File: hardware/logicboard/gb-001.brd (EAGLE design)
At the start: 100 x 76 mm, 4 parts

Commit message: Good one.
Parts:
- removed SV2: (no value), con-ml:ML20L
- moved U$1 41.7 mm to (50.0, 38.0)
- moved SV3 26.0 mm to (50.0, 65.0)
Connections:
- new net GND: SV0.10, SV0.12, SV0.14, SV0.16, SV0.18, SV0.2, SV0.20, SV0.22, SV0.24, SV0.26, SV0.28, SV0.30, SV0.32, SV0.34, SV0.4, SV0.6, SV0.8, SV3.5
- new net NC: SV0.17
- new net T00: SV0.1, SV3.1
- new net T01: SV0.3, SV3.3
- new net T02: SV0.5, SV3.7
- new net T03: SV0.7, SV3.9
- new net T04: SV0.9, SV3.11
- new net T05: SV0.11, SV3.2
- new net T06: SV0.13, SV3.4
- new net T07: SV0.15, SV3.6
- new net T08: SV0.19, SV3.8
- new net T09: SV0.21, SV3.10
- new net T10: SV0.23, SV3.12
- new net T11: SV0.25, SV3.14
- new net T12: SV0.27
- new net T13: SV0.29
- new net T14: SV0.31
- new net T15: SV0.33
- new net VT: SV3.13
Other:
- board text added: "GeekBox 0.0.1-A"
- board text removed: "Pineapple IId 0.0.2-B"

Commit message: Routed.
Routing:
- net GND: track 0.00 -> 96.3 mm
- net T00: track 0.00 -> 74.2 mm
- net T10: track 0.00 -> 70.1 mm
- net T11: track 0.00 -> 69.3 mm
- net T07: track 0.00 -> 65.9 mm
- net T01: track 0.00 -> 65.5 mm
- net T05: track 0.00 -> 63.5 mm
- net T02: track 0.00 -> 60.9 mm
- net T09: track 0.00 -> 60.4 mm
- net T06: track 0.00 -> 59.1 mm
- net T03: track 0.00 -> 55.7 mm
- net T08: track 0.00 -> 55.1 mm
- net T04: track 0.00 -> 53.6 mm

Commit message: Added extra pins.
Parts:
- added JP1: (no value), pinhead:2X04
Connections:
- net GND: now also JP1.2, JP1.4, JP1.6, JP1.8
- net T12: now also JP1.1
- net T13: now also JP1.3
- net T14: now also JP1.5
- net T15: now also JP1.7
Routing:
- net T14: track 0.00 -> 62.4 mm
- net T13: track 0.00 -> 57.5 mm
- net T15: track 0.00 -> 53.4 mm, vias 0 -> 1
- net T12: track 0.00 -> 47.1 mm
- net GND: track 96.3 -> 120.5 mm
- net T07: track 65.9 -> 56.1 mm
- net T11: track 69.3 -> 77.2 mm
- net T01: track 65.5 -> 72.6 mm
- net T10: track 70.1 -> 63.8 mm
- net T06: track 59.1 -> 64.7 mm, vias 0 -> 1
- net T03: track 55.7 -> 58.8 mm
- net T00: track 74.2 -> 76.2 mm
- net T05: track 63.5 -> 65.2 mm
- net T02: track 60.9 -> 62.4 mm

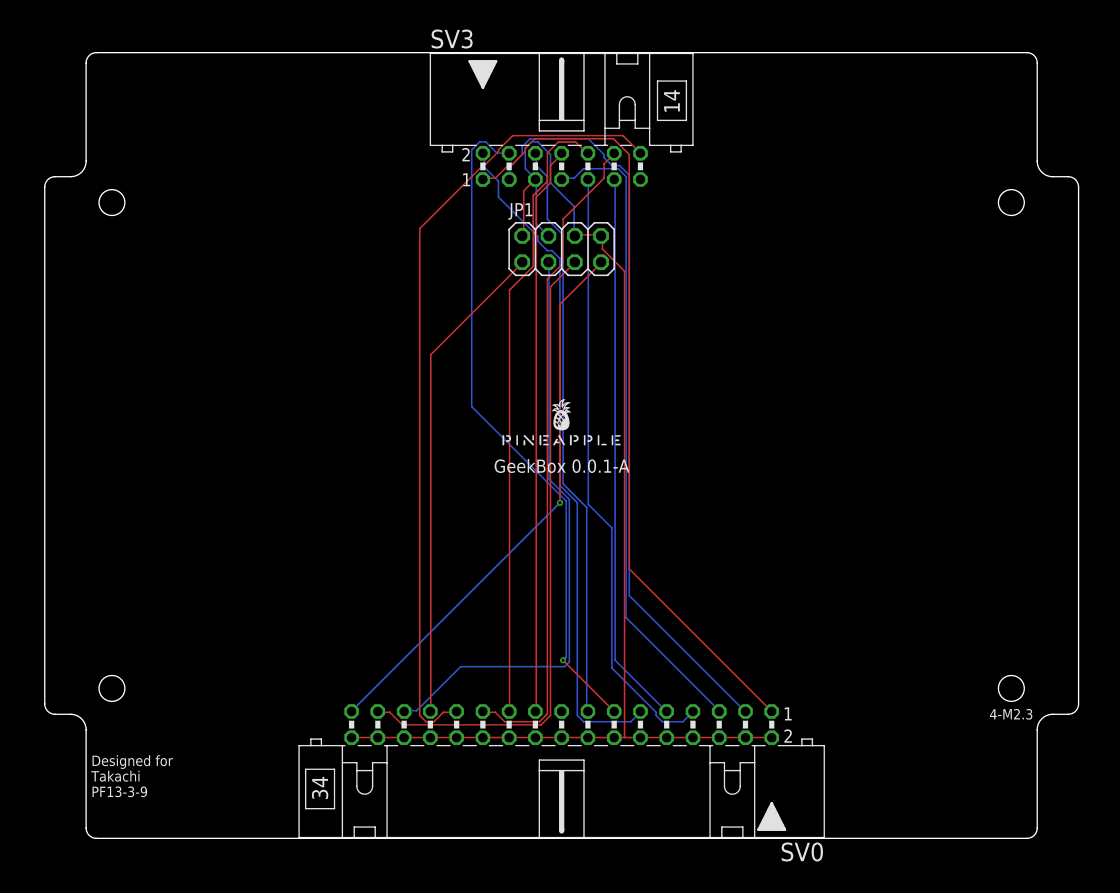
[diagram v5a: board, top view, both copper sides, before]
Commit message: Added PWR led.
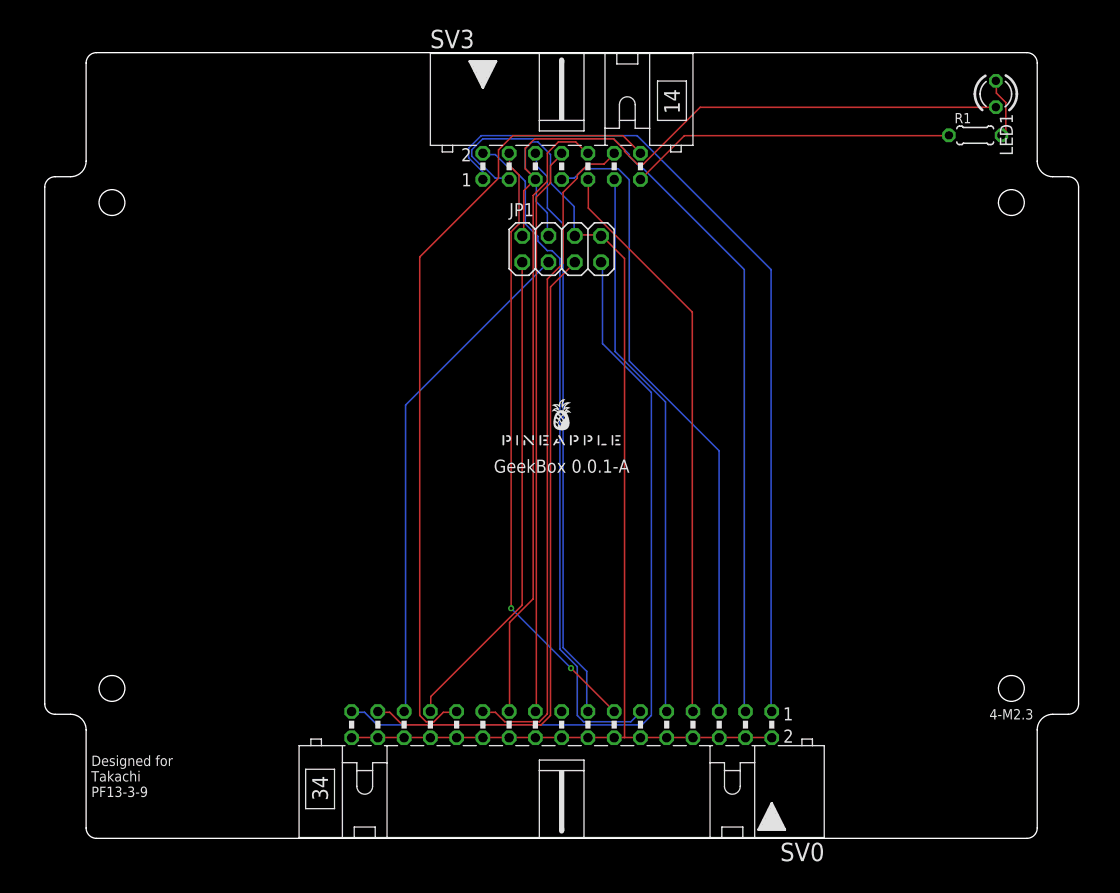
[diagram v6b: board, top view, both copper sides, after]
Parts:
- added LED1: (no value), led:LED3MM
- added R1: (no value), rcl:0204/5
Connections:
- removed net VT: SV3.13
- new net N$2: LED1.A, R1.2
- new net VCC: R1.1, SV3.13
- net GND: now also LED1.K
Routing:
- net GND: track 120.5 -> 173.2 mm
- net VCC: track 0.00 -> 31.6 mm
- net T15: track 53.4 -> 75.8 mm, vias 1 -> 0
- net T13: track 57.5 -> 49.3 mm
- net T01: track 72.6 -> 80.1 mm
- net T06: track 64.7 -> 58.8 mm, vias 1 -> 2
- net N$2: track 0.00 -> 5.83 mm
- net T00: track 76.2 -> 81.5 mm
- net T03: track 58.8 -> 55.7 mm
- net T10: track 63.8 -> 64.7 mm
- net T05: track 65.2 -> 66.0 mm

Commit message: Added GeekPort.
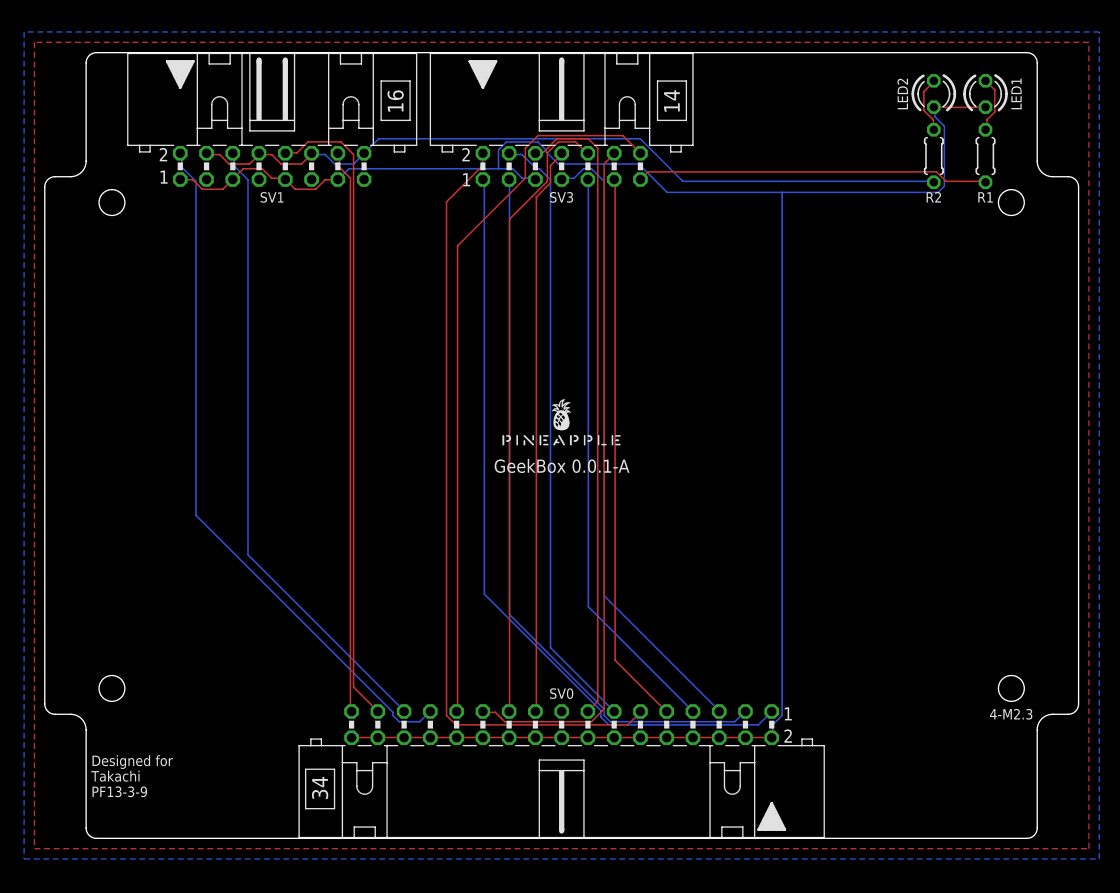
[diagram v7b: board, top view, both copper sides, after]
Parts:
- removed JP1: (no value), pinhead:2X04
- added LED2: (no value), led:LED3MM
- added R2: (no value), rcl:0204/5
- added SV1: (no value), con-ml:ML16L
- moved R1 2.24 mm to (91.0, 66.0), turned to 90 degrees
- moved LED1 1.00 mm to (91.0, 72.0)
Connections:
- new net N$1: LED2.A, R2.2
- new net VCC/2: R2.1, SV1.12, SV1.16, SV1.4, SV1.8
- net GND: now also LED2.K, SV1.1, SV1.13, SV1.5, SV1.9; no longer JP1.2, JP1.4, JP1.6, JP1.8
- net T12: now also SV1.2; no longer JP1.1
- net T13: now also SV1.6; no longer JP1.3
- net T14: now also SV1.10; no longer JP1.5
- net T15: now also SV1.14; no longer JP1.7
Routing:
- net VCC/2: track 0.00 -> 75.4 mm
- net T15: track 75.8 -> 54.6 mm
- net T12: track 47.1 -> 67.2 mm
- net GND: track 173.2 -> 192.4 mm
- net T13: track 49.3 -> 60.9 mm
- net T01: track 80.1 -> 70.0 mm
- net T05: track 66.0 -> 75.5 mm
- net T11: track 77.1 -> 69.6 mm
- net T00: track 81.5 -> 74.2 mm
- net T07: track 56.1 -> 61.9 mm
- net N$1: track 0.00 -> 5.52 mm
- net VCC: track 31.6 -> 34.1 mm
- net T10: track 64.7 -> 66.8 mm
- net T02: track 62.4 -> 60.9 mm
- net T06: track 58.8 -> 59.1 mm, vias 2 -> 0
- added copper zone on layer 1, net GND
- added copper zone on layer 16, net GND

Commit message: Added signal names and silk patterns.
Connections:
- net N$1 renamed VCC2LED
- net N$2 renamed VCCLED
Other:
- board text added: "V"
- board text added: "V/2"
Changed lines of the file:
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@@
 PF13-3-9</text>
 <text x="93.5" y="12" size="1" layer="25" align="center">4-M2.3</text>
+<text x="91" y="75" size="1.27" layer="25" align="center">V</text>
+<text x="86" y="75" size="1.27" layer="25" align="center">V/2</text>
 </plain>
 <attributes>
@@
 <wire x1="57.7596" y1="63.8556" x2="57.62" y2="63.73" width="0.1524" layer="1"/>
 </signal>
-<signal name="N$2">
+<signal name="VCCLED">
 <contactref element="R1" pad="2"/>
 <contactref element="LED1" pad="A"/>
@@
 <wire x1="91.1352" y1="73.152" x2="91" y2="73.27" width="0.1524" layer="1"/>
 </signal>
-<signal name="N$1">
+<signal name="VCC2LED">
 <contactref element="LED2" pad="A"/>
 <contactref element="R2" pad="2"/>
